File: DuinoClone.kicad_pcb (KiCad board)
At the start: 2 copper layers, 0 parts

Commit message: Set design rules
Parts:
- added BT1: Battery 3v, Connector_PinHeader_2.54mm:PinHeader_1x02_P2.54mm_Vertical, F.Cu at (108.7, 60.2)
- added C1: 22pf, Capacitor_SMD:C_0805_2012Metric_Pad1.15x1.40mm_HandSolder, F.Cu at (145.7, 88.9)
- added C2: 22pf, Capacitor_SMD:C_0805_2012Metric_Pad1.15x1.40mm_HandSolder, F.Cu at (146.0, 94.8)
- added C3: 10uf, Capacitor_SMD:C_0805_2012Metric_Pad1.15x1.40mm_HandSolder, F.Cu at (141.2, 99.1)
- added D1: LED, LED_SMD:LED_0805_2012Metric_Pad1.15x1.40mm_HandSolder, F.Cu at (136.5, 98.0)
- added J1: Digital pins, Connector_PinHeader_2.54mm:PinHeader_1x09_P2.54mm_Vertical, F.Cu at (86.5, 60.1)
- added J2: Serial, Connector_PinHeader_2.54mm:PinHeader_1x04_P2.54mm_Vertical, F.Cu at (95.8, 60.1)
- added J3: ICSP, Connector_PinHeader_2.54mm:PinHeader_2x03_P2.54mm_Vertical, F.Cu at (100.5, 60.1)
- added J4: I2C, Connector_PinHeader_2.54mm:PinHeader_1x04_P2.54mm_Vertical, F.Cu at (91.2, 60.1)
- added R1: 330ohm, Resistor_SMD:R_0805_2012Metric_Pad1.15x1.40mm_HandSolder, F.Cu at (145.7, 91.9)
- added R2: 10kohm, Resistor_SMD:R_0805_2012Metric_Pad1.15x1.40mm_HandSolder, F.Cu at (141.2, 96.1)
- added U1: DS1337S+, Package_SO:SO-8_5.3x6.2mm_P1.27mm, F.Cu at (122.1, 97.9)
- added U2: 24LC1025, Package_SO:SOIJ-8_5.3x5.3mm_P1.27mm, F.Cu at (133.4, 93.0)
- added U3: 24LC1025, Package_SO:SOIJ-8_5.3x5.3mm_P1.27mm, F.Cu at (133.4, 86.1)
- added U4: ATMEGA328P-AU, digikey-footprints:TQFP-32_7x7mm, F.Cu at (122.4, 88.3)
- added Y1: Crystal 32MHz, Crystal:Crystal_SMD_MicroCrystal_CC7V-T1A-2Pin_3.2x1.5mm_HandSoldering, F.Cu at (130.8, 98.2)
- added Y2: Crystal 16MHz, Crystal:Crystal_SMD_5032-2Pin_5.0x3.2mm_HandSoldering, F.Cu at (143.8, 85.0)
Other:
- net class Power added: clearance 0.2, trace_width 0.3, via_dia 1, via_drill 0.6

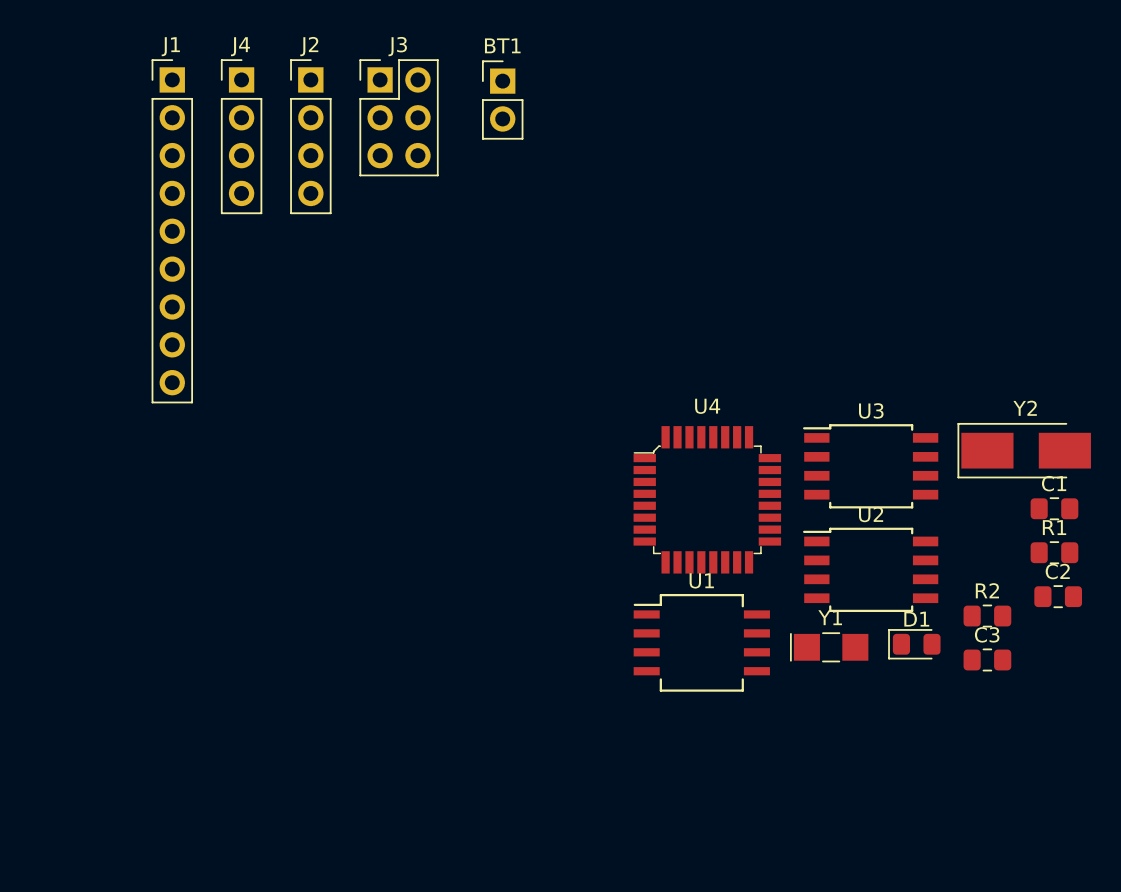
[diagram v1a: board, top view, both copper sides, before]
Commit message: First version of pcb component placement
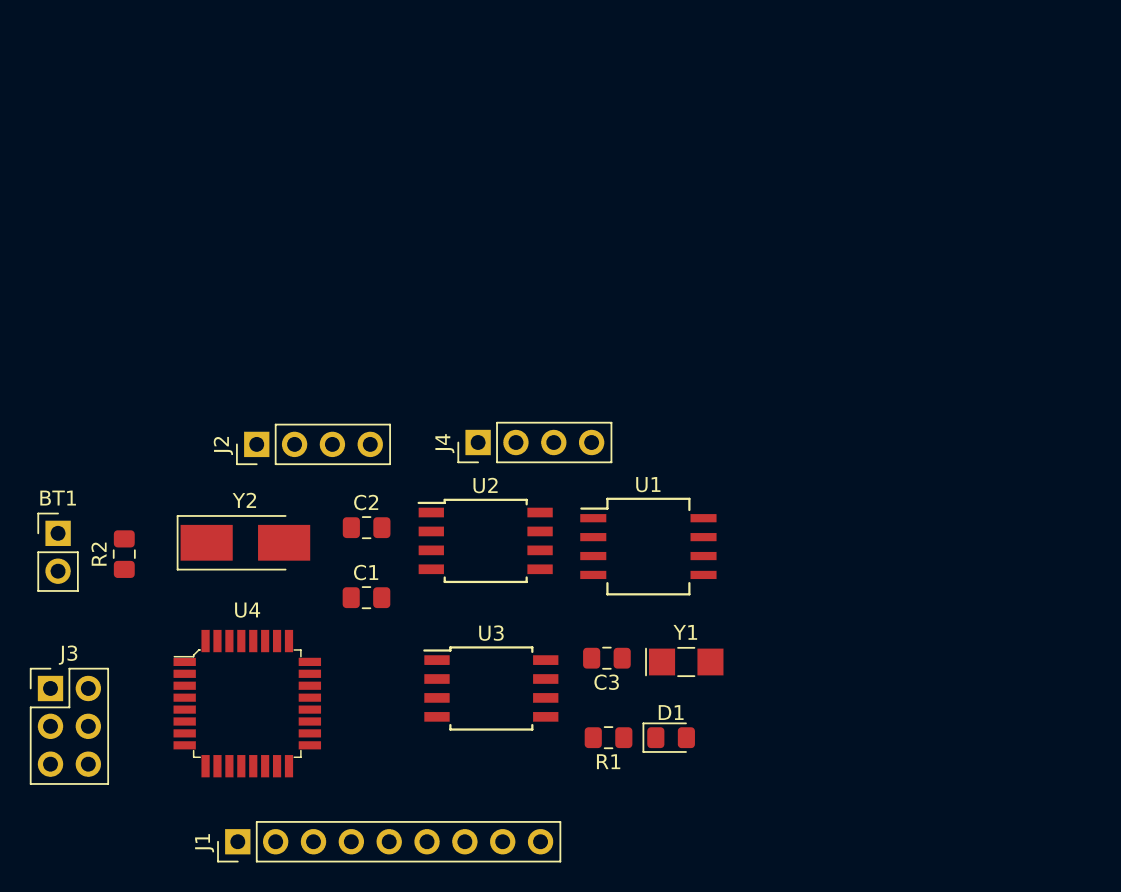
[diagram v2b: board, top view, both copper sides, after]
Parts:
- moved R2 58.1 mm to (83.3, 91.9), turned to 90 degrees
- moved Y2 52.8 mm to (91.4, 91.2)
- moved J1 51.3 mm to (90.9, 111.3), turned to 90 degrees
- moved C2 46.6 mm to (99.6, 90.2)
- moved C1 46.6 mm to (99.6, 94.9)
- moved J3 46.5 mm to (78.4, 101.0)
- moved BT1 42.6 mm to (78.9, 90.6)
- moved U4 33.8 mm to (91.6, 102.0)
- moved R1 32.4 mm to (115.8, 104.3), turned to 180 degrees
- moved U3 29.5 mm to (108.0, 101.0)
- moved J4 29.1 mm to (107.1, 84.5), turned to 90 degrees
- moved U2 25.9 mm to (107.6, 91.1)
- moved C3 25.5 mm to (115.7, 98.9), turned to 180 degrees
- moved J2 24.7 mm to (92.2, 84.6), turned to 90 degrees
- moved D1 17.6 mm to (120.0, 104.3)
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
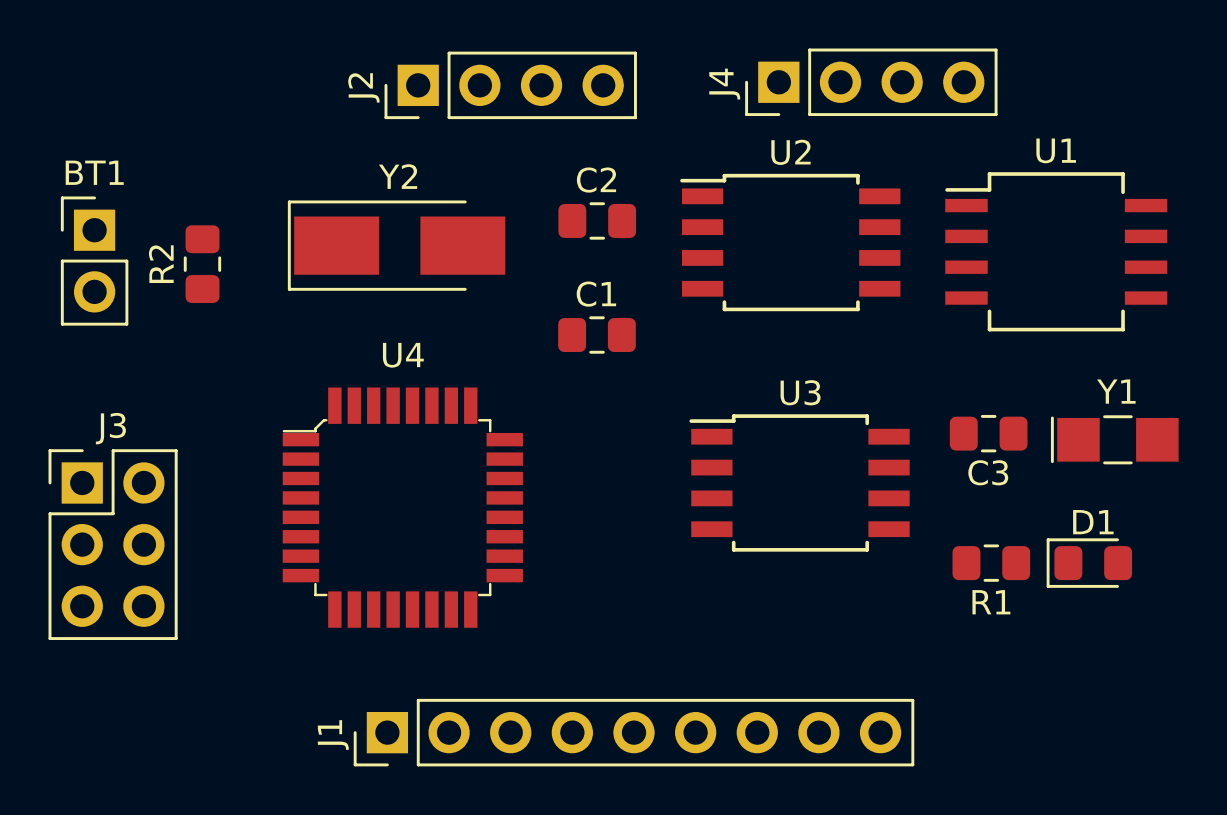
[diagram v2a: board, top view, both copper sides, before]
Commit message: 2nd version pcb component placement
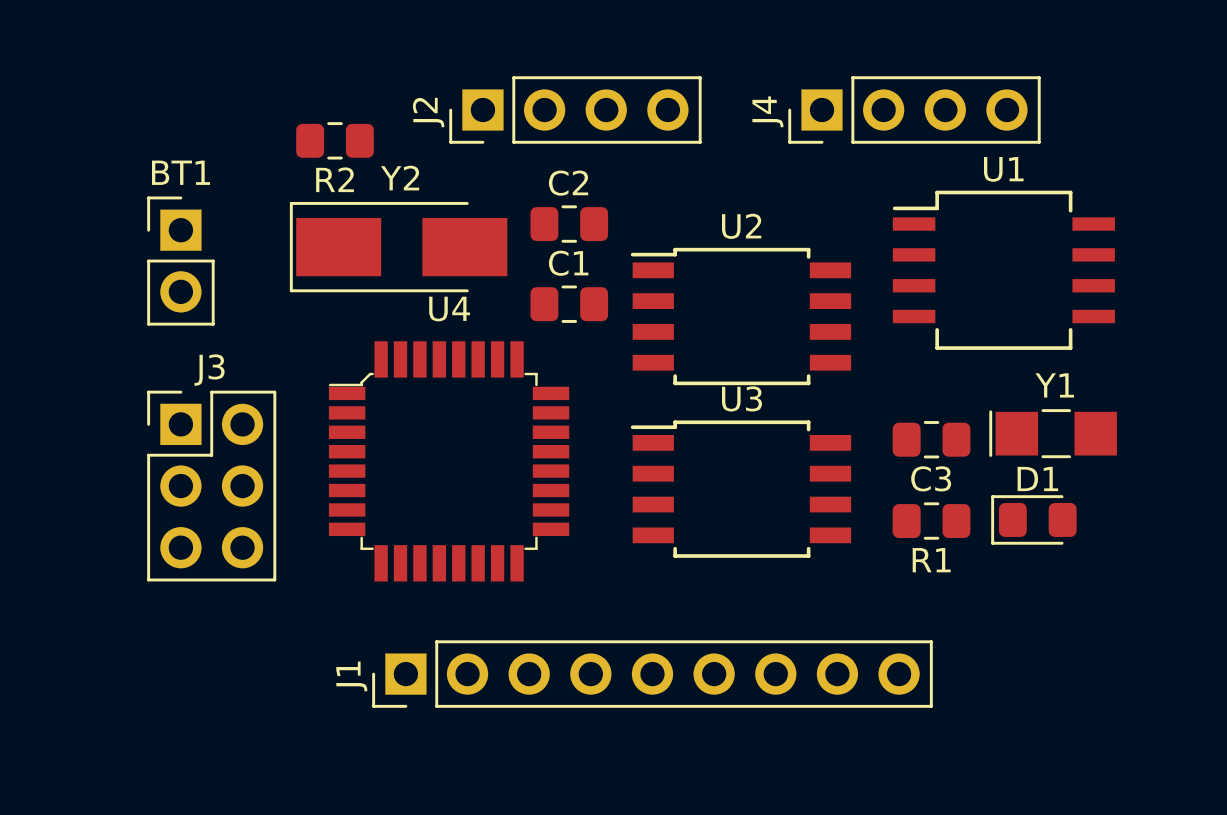
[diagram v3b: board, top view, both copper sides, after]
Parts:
- moved R2 7.46 mm to (88.8, 86.9), turned to 180 degrees
- moved J3 4.73 mm to (82.4, 98.6)
- moved U2 3.66 mm to (105.5, 94.1)
- moved BT1 3.56 mm to (82.4, 90.6)
- moved R1 3.01 mm to (113.4, 102.5)
- moved D1 2.90 mm to (117.7, 102.5)
- moved J2 2.85 mm to (94.9, 85.6)
- moved U4 2.69 mm to (93.5, 100.1)
- moved Y1 2.55 mm to (118.5, 98.9)
- moved J1 2.53 mm to (91.7, 108.8)
- moved U3 2.43 mm to (105.5, 101.2)
- moved C3 2.37 mm to (113.4, 99.2)
- moved U1 2.29 mm to (116.3, 92.2)
- moved J4 2.11 mm to (108.8, 85.6)
- moved C1 1.71 mm to (98.4, 93.6)
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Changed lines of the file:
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@@
   )
   (module Connector_PinHeader_2.54mm:PinHeader_1x02_P2.54mm_Vertical (layer F.Cu)
-    (at 78.867 90.551)
+    (at 82.423 90.551)
     (descr "Through hole straight pin header, 1x02, 2.54mm pitch, single row")
     (tags "Through hole pin header THT 1x02 2.54mm single row")
@@
   )
   (module Capacitor_SMD:C_0805_2012Metric_Pad1.15x1.40mm_HandSolder (layer F.Cu)
-    (at 99.568 94.869)
+    (at 98.425 93.599)
     (descr "Capacitor SMD 0805 (2012 Metric), square (rectangular) end terminal, IPC_7351 nominal with elongated pad for handsoldering. (Body size source: https://docs.google.com/spreadsheets/d/1BsfQQcO9C6DZCsRaXUlFlo91Tg2WpOkGARC1WS5S8t0/edit?usp=sharing), generated with kicad-footprint-generator")
     (tags "capacitor handsolder")
@@
   )
   (module Capacitor_SMD:C_0805_2012Metric_Pad1.15x1.40mm_HandSolder (layer F.Cu)
-    (at 99.577 90.17)
+    (at 98.425 90.297)
     (descr "Capacitor SMD 0805 (2012 Metric), square (rectangular) end terminal, IPC_7351 nominal with elongated pad for handsoldering. (Body size source: https://docs.google.com/spreadsheets/d/1BsfQQcO9C6DZCsRaXUlFlo91Tg2WpOkGARC1WS5S8t0/edit?usp=sharing), generated with kicad-footprint-generator")
     (tags "capacitor handsolder")
@@
   )
   (module Capacitor_SMD:C_0805_2012Metric_Pad1.15x1.40mm_HandSolder (layer F.Cu)
-    (at 115.706 98.933 180)
+    (at 113.352 99.183 180)
     (descr "Capacitor SMD 0805 (2012 Metric), square (rectangular) end terminal, IPC_7351 nominal with elongated pad for handsoldering. (Body size source: https://docs.google.com/spreadsheets/d/1BsfQQcO9C6DZCsRaXUlFlo91Tg2WpOkGARC1WS5S8t0/edit?usp=sharing), generated with kicad-footprint-generator")
     (tags "capacitor handsolder")
@@
   )
   (module LED_SMD:LED_0805_2012Metric_Pad1.15x1.40mm_HandSolder (layer F.Cu)
-    (at 120.015 104.267)
+    (at 117.729 102.489)
     (descr "LED SMD 0805 (2012 Metric), square (rectangular) end terminal, IPC_7351 nominal, (Body size source: https://docs.google.com/spreadsheets/d/1BsfQQcO9C6DZCsRaXUlFlo91Tg2WpOkGARC1WS5S8t0/edit?usp=sharing), generated with kicad-footprint-generator")
     (tags "LED handsolder")
@@
   )
   (module Connector_PinHeader_2.54mm:PinHeader_1x09_P2.54mm_Vertical (layer F.Cu)
-    (at 90.932 111.252 90)
+    (at 91.694 108.839 90)
     (descr "Through hole straight pin header, 1x09, 2.54mm pitch, single row")
     (tags "Through hole pin header THT 1x09 2.54mm single row")
@@
   )
   (module Connector_PinHeader_2.54mm:PinHeader_1x04_P2.54mm_Vertical (layer F.Cu)
-    (at 92.202 84.582 90)
+    (at 94.869 85.598 90)
     (descr "Through hole straight pin header, 1x04, 2.54mm pitch, single row")
     (tags "Through hole pin header THT 1x04 2.54mm single row")
@@
   )
   (module Connector_PinHeader_2.54mm:PinHeader_2x03_P2.54mm_Vertical (layer F.Cu)
-    (at 78.359 100.965)
+    (at 82.423 98.552)
     (descr "Through hole straight pin header, 2x03, 2.54mm pitch, double rows")
     (tags "Through hole pin header THT 2x03 2.54mm double row")
@@
   )
   (module Connector_PinHeader_2.54mm:PinHeader_1x04_P2.54mm_Vertical (layer F.Cu)
-    (at 107.061 84.455 90)
+    (at 108.839 85.598 90)
     (descr "Through hole straight pin header, 1x04, 2.54mm pitch, single row")
     (tags "Through hole pin header THT 1x04 2.54mm single row")
@@
   )
   (module Resistor_SMD:R_0805_2012Metric_Pad1.15x1.40mm_HandSolder (layer F.Cu)
-    (at 115.815 104.267 180)
+    (at 113.352 102.534 180)
     (descr "Resistor SMD 0805 (2012 Metric), square (rectangular) end terminal, IPC_7351 nominal with elongated pad for handsoldering. (Body size source: https://docs.google.com/spreadsheets/d/1BsfQQcO9C6DZCsRaXUlFlo91Tg2WpOkGARC1WS5S8t0/edit?usp=sharing), generated with kicad-footprint-generator")
     (tags "resistor handsolder")
@@
   )
   (module Resistor_SMD:R_0805_2012Metric_Pad1.15x1.40mm_HandSolder (layer F.Cu)
-    (at 83.312 91.948 90)
+    (at 88.773 86.868 180)
     (descr "Resistor SMD 0805 (2012 Metric), square (rectangular) end terminal, IPC_7351 nominal with elongated pad for handsoldering. (Body size source: https://docs.google.com/spreadsheets/d/1BsfQQcO9C6DZCsRaXUlFlo91Tg2WpOkGARC1WS5S8t0/edit?usp=sharing), generated with kicad-footprint-generator")
     (tags "resistor handsolder")
     (attr smd)
-    (fp_text reference R2 (at 0 -1.65 90) (layer F.SilkS)
-      (effects (font (size 1 1) (thickness 0.15)))
-    )
-    (fp_text value 10kohm (at 0 1.65 90) (layer F.Fab)
-      (effects (font (size 1 1) (thickness 0.15)))
-    )
-    (fp_text user %R (at 0 0 90) (layer F.Fab)
+    (fp_text reference R2 (at 0 -1.65) (layer F.SilkS)
+      (effects (font (size 1 1) (thickness 0.15)))
+    )
+    (fp_text value 10kohm (at 0 1.65) (layer F.Fab)
+      (effects (font (size 1 1) (thickness 0.15)))
+    )
+    (fp_text user %R (at 0 0) (layer F.Fab)
       (effects (font (size 0.5 0.5) (thickness 0.08)))
     )
@@
     (fp_line (start -1 -0.6) (end 1 -0.6) (layer F.Fab) (width 0.1))
     (fp_line (start -1 0.6) (end -1 -0.6) (layer F.Fab) (width 0.1))
-    (pad 2 smd roundrect (at 1.025 0 90) (size 1.15 1.4) (layers F.Cu F.Paste F.Mask) (roundrect_rratio 0.217391)
-      (net 1 /Vcc))
-    (pad 1 smd roundrect (at -1.025 0 90) (size 1.15 1.4) (layers F.Cu F.Paste F.Mask) (roundrect_rratio 0.217391)
+    (pad 2 smd roundrect (at 1.025 0 180) (size 1.15 1.4) (layers F.Cu F.Paste F.Mask) (roundrect_rratio 0.217391)
+      (net 1 /Vcc))
+    (pad 1 smd roundrect (at -1.025 0 180) (size 1.15 1.4) (layers F.Cu F.Paste F.Mask) (roundrect_rratio 0.217391)
       (net 18 /RESET))
     (model ${KISYS3DMOD}/Resistor_SMD.3dshapes/R_0805_2012Metric.wrl
@@
   )
   (module Package_SO:SO-8_5.3x6.2mm_P1.27mm (layer F.Cu)
-    (at 118.491 91.44)
+    (at 116.332 92.202)
     (descr "8-Lead Plastic Small Outline, 5.3x6.2mm Body (http://www.ti.com.cn/cn/lit/ds/symlink/tl7705a.pdf)")
     (tags "SOIC 1.27")
@@
   )
   (module Package_SO:SOIJ-8_5.3x5.3mm_P1.27mm (layer F.Cu)
-    (at 107.569 91.059)
+    (at 105.537 94.107)
     (descr "8-Lead Plastic Small Outline (SM) - Medium, 5.28 mm Body [SOIC] (see Microchip Packaging Specification 00000049BS.pdf)")
     (tags "SOIC 1.27")
@@
   )
   (module Package_SO:SOIJ-8_5.3x5.3mm_P1.27mm (layer F.Cu)
-    (at 107.95 100.965)
+    (at 105.537 101.219)
     (descr "8-Lead Plastic Small Outline (SM) - Medium, 5.28 mm Body [SOIC] (see Microchip Packaging Specification 00000049BS.pdf)")
     (tags "SOIC 1.27")
@@
   )
   (module digikey-footprints:TQFP-32_7x7mm (layer F.Cu)
-    (at 91.567 101.981)
+    (at 93.472 100.076)
     (descr http://www.atmel.com/Images/Atmel-8826-SEEPROM-PCB-Mounting-Guidelines-Surface-Mount-Packages-ApplicationNote.pdf)
     (fp_text reference U4 (at 0 -6.25) (layer F.SilkS)
@@
   )
   (module Crystal:Crystal_SMD_MicroCrystal_CC7V-T1A-2Pin_3.2x1.5mm_HandSoldering (layer F.Cu)
-    (at 121.031 99.187)
+    (at 118.491 98.933)
     (descr "SMD Crystal MicroCrystal CC7V-T1A/CM7V-T1A series http://www.microcrystal.com/images/_Product-Documentation/01_TF_ceramic_Packages/01_Datasheet/CC1V-T1A.pdf, hand-soldering, 3.2x1.5mm^2 package")
     (tags "SMD SMT crystal hand-soldering")
@@
   )
   (module Crystal:Crystal_SMD_5032-2Pin_5.0x3.2mm_HandSoldering (layer F.Cu)
-    (at 91.44 91.186)
+    (at 91.523 91.247)
     (descr "SMD Crystal SERIES SMD2520/2 http://www.icbase.com/File/PDF/HKC/HKC00061008.pdf, hand-soldering, 5.0x3.2mm^2 package")
     (tags "SMD SMT crystal hand-soldering")
